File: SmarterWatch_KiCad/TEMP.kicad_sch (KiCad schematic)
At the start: 2 parts, among them U7 TMP117xxDRV

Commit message: Footprint Stuff
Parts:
- U7: footprint Package_SON:WSON-6-1EP_2x2mm_P0.65mm_EP1x1.6mm -> (none)
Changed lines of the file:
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@@
 			)
 		)
-		(property "Footprint" "Package_SON:WSON-6-1EP_2x2mm_P0.65mm_EP1x1.6mm"
+		(property "Footprint" ""
 			(at 149.86 114.3 0)
 			(effects

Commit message: new
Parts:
- U7: footprint (none) -> Custom_Foot:SON65P200X200X80-7N
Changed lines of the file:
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@@
 			)
 		)
-		(property "Footprint" ""
+		(property "Footprint" "Custom_Foot:SON65P200X200X80-7N"
 			(at 149.86 114.3 0)
 			(effects

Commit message: Jumper Footprint
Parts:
- U7: footprint Custom_Foot:SON65P200X200X80-7N -> (none)
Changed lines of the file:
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@@
 			)
 		)
-		(property "Footprint" "Custom_Foot:SON65P200X200X80-7N"
+		(property "Footprint" ""
 			(at 149.86 114.3 0)
 			(effects

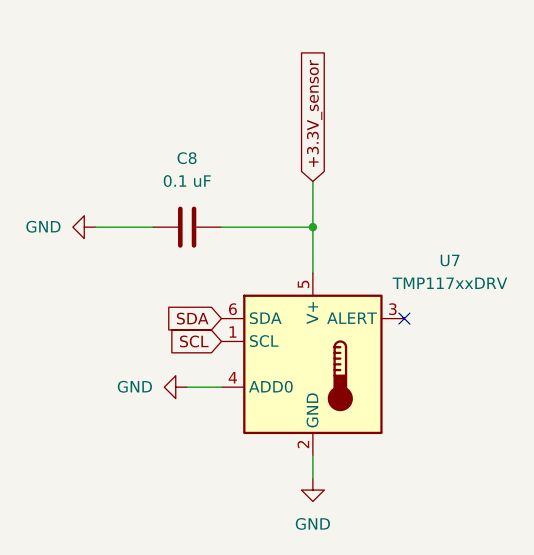
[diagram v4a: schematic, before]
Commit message: added pad to symbol
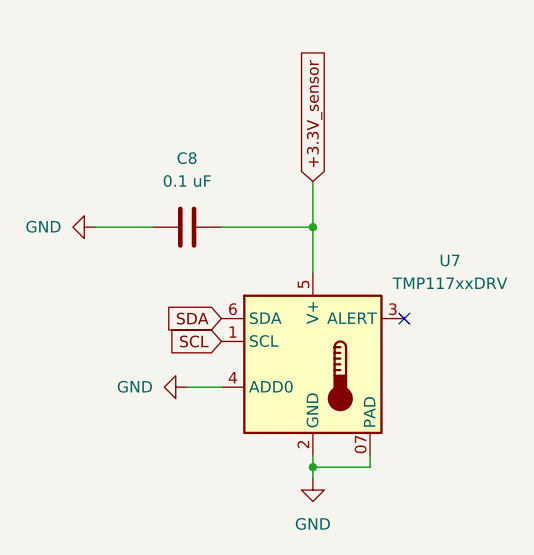
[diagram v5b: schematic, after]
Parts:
- U7: footprint (none) -> Custom_Foot:SON65P200X200X80-7N
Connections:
- net GND: now also U7.07 (PAD)
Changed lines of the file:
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@@
 	(paper "A4")
+	(junction
+		(at 148.59 116.84)
+		(diameter 0)
+		(color 0 0 0 0)
+	)
 	(junction
 		(at 148.59 90.17)
@@
 	(wire
 		(pts
+			(xy 148.59 116.84) (xy 154.94 116.84)
+		)
+		(stroke
+			(width 0)
+			(type default)
+		)
+	)
+	(wire
+		(pts
 			(xy 138.43 90.17) (xy 148.59 90.17)
 		)
@@
 	(wire
 		(pts
-			(xy 148.59 115.57) (xy 148.59 118.11)
+			(xy 148.59 115.57) (xy 148.59 116.84)
 		)
 		(stroke
@@
 	(wire
 		(pts
+			(xy 154.94 115.57) (xy 154.94 116.84)
+		)
+		(stroke
+			(width 0)
+			(type default)
+		)
+	)
+	(wire
+		(pts
 			(xy 148.59 85.09) (xy 148.59 90.17)
+		)
+		(stroke
+			(width 0)
+			(type default)
+		)
+	)
+	(wire
+		(pts
+			(xy 148.59 116.84) (xy 148.59 118.11)
 		)
 		(stroke
@@
 			)
 		)
-		(property "Footprint" ""
+		(property "Footprint" "Custom_Foot:SON65P200X200X80-7N"
 			(at 149.86 114.3 0)
 			(effects
@@
 		(pin "3"
 		)
+		(pin "07"
+		)
 		(instances

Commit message: via stuff
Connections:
- net +3.3V_sensor renamed +3.3V
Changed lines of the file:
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@@
-		)
-	)
-	(global_label "+3.3V_sensor"
-		(shape input)
-		(at 148.59 85.09 90)
-		(fields_autoplaced yes)
-		(effects
-			(font
-				(size 1.27 1.27)
-			)
-			(justify left)
-		)
-		(property "Intersheetrefs" "${INTERSHEET_REFS}"
-			(at 148.59 69.2234 90)
-			(effects
-				(font
-					(size 1.27 1.27)
-				)
-				(justify left)
-				(hide yes)
-			)
 		)
 	)
@@
 					(unit 1)
 				)
+			)
+		)
+	)
+	(symbol
+		(lib_id "power:+3.3V")
+		(at 148.59 85.09 0)
+		(unit 1)
+		(exclude_from_sim no)
+		(in_bom yes)
+		(on_board yes)
+		(dnp no)
+		(fields_autoplaced yes)
+		(property "Reference" "#PWR0107"
+			(at 148.59 88.9 0)
+			(effects
+				(font
+					(size 1.27 1.27)
+				)
+				(hide yes)
+			)
+		)
+		(property "Value" "+3.3V"
+			(at 148.59 80.01 0)
+			(effects
+				(font
+					(size 1.27 1.27)
+				)
+			)
+		)
+		(property "Footprint" ""
+			(at 148.59 85.09 0)
+			(effects
+				(font
+					(size 1.27 1.27)
+				)
+				(hide yes)
+			)
+		)
+		(property "Datasheet" ""
+			(at 148.59 85.09 0)
+			(effects
+				(font
+					(size 1.27 1.27)
+				)
+				(hide yes)
+			)
+		)
+		(property "Description" "Power symbol creates a global label with name \"+3.3V\""
+			(at 148.59 85.09 0)
+			(effects
+				(font
+					(size 1.27 1.27)
+				)
+				(hide yes)
+			)
+		)
+		(pin "1"
+		)
+		(instances
+			(project ""
+				(path "/52181fb0-1be8-41da-83b2-7d5a62778ff4/01b5dd88-d733-4c4b-897c-9901ed06fbc3"
+					(reference "#PWR0107")
+					(unit 1)
+				)
